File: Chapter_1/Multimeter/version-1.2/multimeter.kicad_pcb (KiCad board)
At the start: 2 copper layers, 148.8 x 87.8 mm, 56 parts, among them J1 Screw_Terminal_01x02, J2 Conn_01x02_Socket, Q1 IRLZ44N, Q17 BC547, Q18 BC547, Q19 BC547, Q20 BC547, Q22 BC547, Q23 BC547, Q24 BC547, Q25 BC547, Q26 BC547, Q27 BC547, Q28 BC547, Q29 BC547, Q30 BC547, Q31 BC547, Q32 BC547, Q33 IRLZ44N, Q34 IRLZ44N, SW1 SW_DPST_x2, SW2 SW_DPST_x2, SW3 SW_DPST_x2

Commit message: final version1.2
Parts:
- added H1: MountingHole, MountingHole:MountingHole_3.2mm_M3, F.Cu at (46.0, 40.2)
- added H2: MountingHole, MountingHole:MountingHole_3.2mm_M3, F.Cu at (183.0, 39.8)
- added H3: MountingHole, MountingHole:MountingHole_3.2mm_M3, F.Cu at (182.2, 115.2)
- added H4: MountingHole, MountingHole:MountingHole_3.2mm_M3, F.Cu at (45.2, 115.8)
- added J3: Screw_Terminal_01x02, TerminalBlock:TerminalBlock_MaiXu_MX126-5.0-02P_1x02_P5.00mm, F.Cu at (47.2, 57.0)
- added R3: 10K, Resistor_THT:R_Axial_DIN0309_L9.0mm_D3.2mm_P12.70mm_Horizontal, F.Cu at (68.9, 60.0)
- added R33: 10K, Resistor_THT:R_Axial_DIN0309_L9.0mm_D3.2mm_P12.70mm_Horizontal, F.Cu at (138.4, 97.5)
- added R4: 10K, Resistor_THT:R_Axial_DIN0309_L9.0mm_D3.2mm_P12.70mm_Horizontal, F.Cu at (67.4, 90.8)
- added R5: 10K, Resistor_THT:R_Axial_DIN0309_L9.0mm_D3.2mm_P12.70mm_Horizontal, F.Cu at (107.3, 51.8)
- added R6: 10K, Resistor_THT:R_Axial_DIN0309_L9.0mm_D3.2mm_P12.70mm_Horizontal, F.Cu at (100.9, 94.5)
- J1: footprint TerminalBlock:TerminalBlock_Xinya_XY308-2.54-2P_1x02_P2.54mm_Horizontal -> TerminalBlock:TerminalBlock_MaiXu_MX126-5.0-02P_1x02_P5.00mm
- J2: footprint Connector_PinSocket_2.54mm:PinSocket_1x02_P2.54mm_Vertical -> TerminalBlock:TerminalBlock_MaiXu_MX126-5.0-02P_1x02_P5.00mm
- R29: value 5K -> 100K
- R30: value 1_Ohm -> 0.015 Ohm
- moved D7 7.24 mm to (129.5, 78.2)
- moved R13 7.15 mm to (69.9, 54.2)
- moved Q23 6.37 mm to (87.2, 59.2)
- moved R9 6.20 mm to (68.7, 85.8)
- moved Q19 6.16 mm to (85.1, 90.0)
- moved D6 6.15 mm to (146.3, 43.5)
- moved R19 5.62 mm to (106.9, 45.5)
- moved R23 5.04 mm to (100.8, 89.2)
- moved R27 4.92 mm to (138.7, 92.0)
- moved Q26 4.88 mm to (125.4, 50.2)
- moved Q17 4.57 mm to (81.5, 101.2)
- moved Q18 4.57 mm to (81.4, 107.2)
- moved R1 4.57 mm to (61.7, 102.2)
- moved R8 4.57 mm to (61.7, 107.7)
- moved R7 4.57 mm to (61.5, 95.7)
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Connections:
- J1 pad 2: /INPUT_NEGATIVE -> GND
- J2 pad 2: /INPUT_NEGATIVE -> GND
- Q17 pad 1: /NAND_OUTPUT -> /SIGNAL_ALLOWED_TO_MEASURER
- Q19 pad 2: /NAND_OUTPUT -> Net-(Q19-B)
- Q23 pad 2: Net-(Q20-C) -> Net-(Q23-B)
- Q26 pad 2: Net-(Q24-C) -> Net-(Q26-B)
- Q29 pad 2: Net-(Q27-C) -> Net-(Q29-B)
- Q32 pad 2: Net-(Q30-C) -> Net-(Q32-B)
- Q34 pad 3: /INPUT_NEGATIVE -> GND
- R17 pad 1: /NAND_OUTPUT -> /SIGNAL_ALLOWED_TO_MEASURER
- R21 pad 1: /NAND_OUTPUT -> /SIGNAL_ALLOWED_TO_MEASURER
- R7 pad 2: /NAND_OUTPUT -> /SIGNAL_ALLOWED_TO_MEASURER
- SW1 pad 1: VCC -> /SIGNAL_POWER_BUTTON
- SW2 pad 1: VCC -> /SIGNAL_POWER_BUTTON
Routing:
- net /SIGNAL_ALLOWED_TO_MEASURER: track 0.00 -> 84.5 mm
- net /NAND_OUTPUT: track 73.4 -> 0.00 mm
- net /INPUT_NEGATIVE: track 49.8 -> 0.00 mm
- net Net-(D6-K): track 121.3 -> 85.4 mm
- net /SIGNAL_POWER_BUTTON: track 192.0 -> 226.4 mm
- net Net-(D5-A): track 129.1 -> 95.1 mm, vias 0 -> 1
- net VCC: track 228.4 -> 254.5 mm, vias 8 -> 4
- net /SIGNAL_VOLTMETER: track 46.0 -> 59.6 mm
- net Net-(J1-Pin_1): track 59.5 -> 47.0 mm
- net /SIGNAL_AMMETER: track 69.8 -> 81.9 mm
- net /SIGNAL_MEASURING_AMPS: track 104.0 -> 96.3 mm, vias 2 -> 0
- net Net-(Q33-D): track 7.62 -> 0.00 mm
- net /INPUT_POSITIVE: track 81.3 -> 74.7 mm
- net Net-(Q29-B): track 0.00 -> 6.39 mm
- net Net-(Q32-B): track 0.00 -> 6.39 mm
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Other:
- board text added: "AmMeter"
- board text added: "VoltMeter"

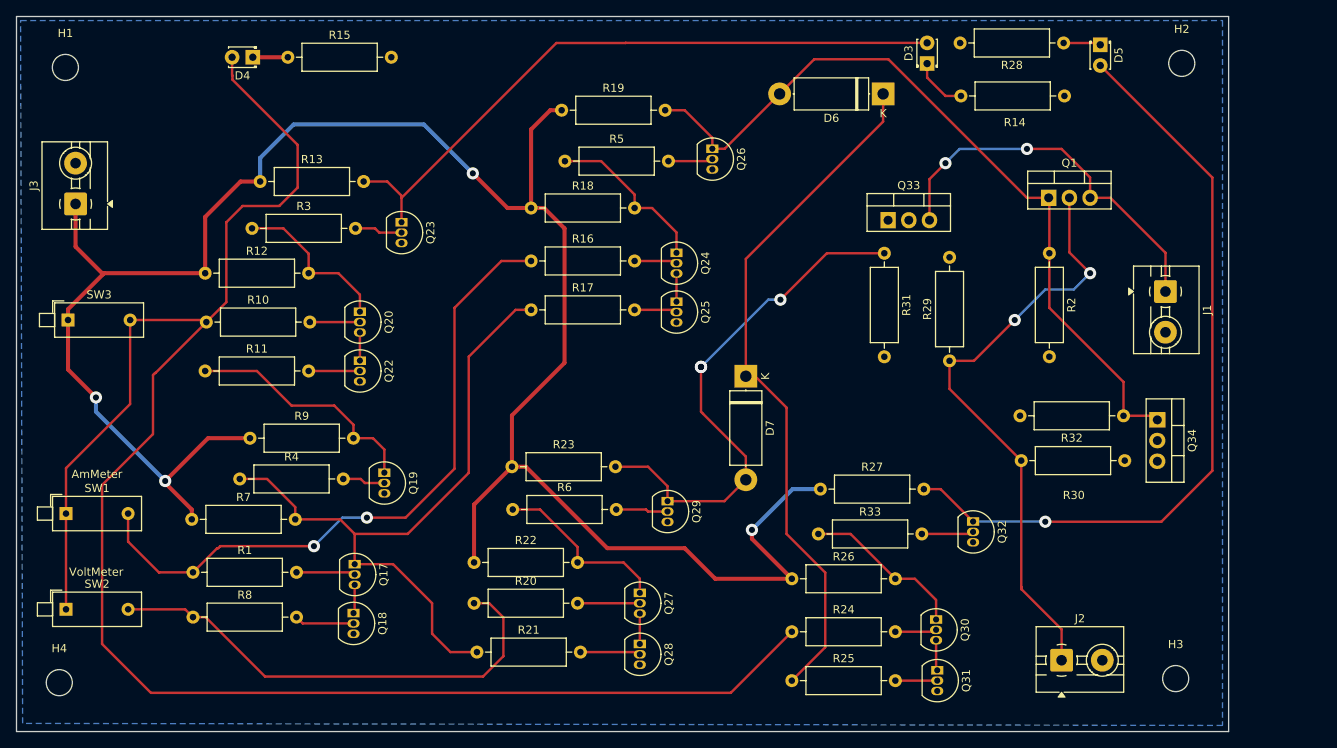
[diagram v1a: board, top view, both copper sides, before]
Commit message: pcb adjusted size
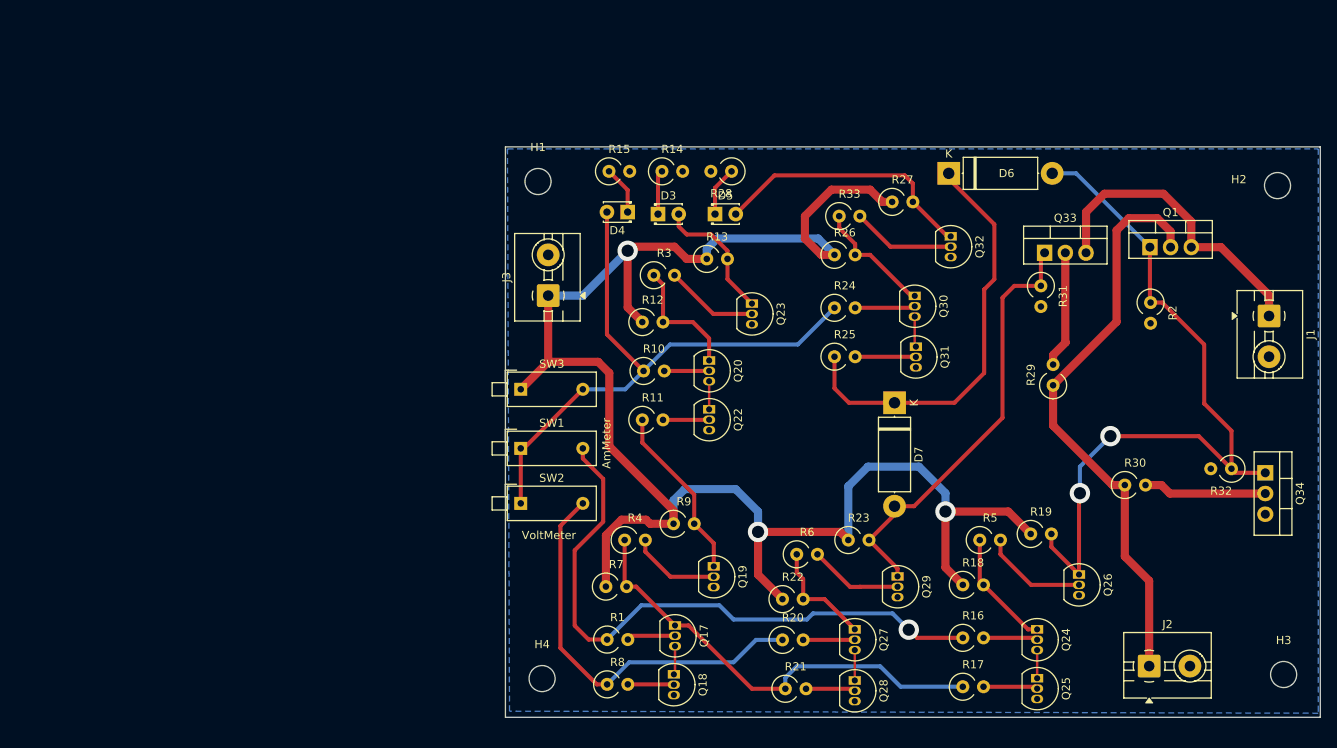
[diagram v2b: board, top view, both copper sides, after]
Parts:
- R1, R10, R11, R12, R13, R14, R15, R16, R17, R18, R19, R2, R20, R21, R22, R23, R24, R25, R26, R27, R28, R29, R3, R30, R31, R32, R33, R4, R5, R6, R7, R8, R9: footprint Resistor_THT:R_Axial_DIN0309_L9.0mm_D3.2mm_P12.70mm_Horizontal -> Resistor_THT:R_Axial_DIN0309_L9.0mm_D3.2mm_P2.54mm_Vertical
- moved R19 77.6 mm to (164.5, 97.5)
- moved R16 70.3 mm to (156.1, 110.2)
- moved R17 70.3 mm to (156.1, 116.2)
- moved R18 70.3 mm to (156.1, 103.8)
- moved Q26 69.0 mm to (170.4, 102.5)
- moved R5 68.9 mm to (158.2, 98.2)
- moved Q24 64.0 mm to (165.2, 109.2)
- moved Q25 64.0 mm to (165.2, 115.2)
- moved H1 59.7 mm to (104.0, 54.2)
- moved H4 59.3 mm to (104.5, 115.2)
- moved J3 59.1 mm to (105.2, 68.2)
- moved SW2 57.3 mm to (101.9, 93.8)
- moved SW1 56.4 mm to (101.9, 87.0)
- moved SW3 56.2 mm to (101.9, 79.8)
- moved R13 55.6 mm to (124.7, 63.8)
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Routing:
- net /SIGNAL_POWER_BUTTON: track 226.4 -> 73.8 mm
- net /SIGNAL_NOT_ALLOWED: track 81.0 -> 16.5 mm
- net Net-(D5-A): track 95.1 -> 32.8 mm, vias 1 -> 0
- net VCC: track 254.5 -> 211.6 mm, vias 4 -> 3
- net Net-(D6-K): track 85.4 -> 51.8 mm
- net /SIGNAL_ALLOWED_TO_MEASURER: track 84.5 -> 55.2 mm
- net Net-(Q34-D): track 0.00 -> 15.1 mm
- net Net-(Q33-D): track 0.00 -> 14.4 mm
- net /SIGNAL_MEASURING_VOLTS: track 64.3 -> 53.4 mm, vias 3 -> 0
- net /SIGNAL_VOLTMETER: track 59.6 -> 50.2 mm
- net Net-(J1-Pin_1): track 47.0 -> 37.9 mm, vias 2 -> 0
- net Net-(Q27-C): track 22.0 -> 13.7 mm
- net /SIGNAL_DUAL-METER: track 29.8 -> 21.6 mm
- net Net-(Q26-B): track 5.49 -> 12.9 mm
- net Net-(Q32-B): track 6.39 -> 12.7 mm
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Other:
- board size 148.8 x 87.8 mm -> 100 x 70 mm
